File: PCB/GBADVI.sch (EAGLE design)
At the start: 77 parts, among them IC2 AMS1117-3.3V, IC3 AMS1117-1.2V, J1 47151-1081HDMI-001, Q1 IRF7319TR, U1 W25Q64JVSSIQ, U2 SN74LVC245APWR, U3 SN74LVC245APWR, U4 52271-1469, U5 FH12A-40S-0.5SH(55), U7 MT48LC16M16A2TG-6A_IT:GTR

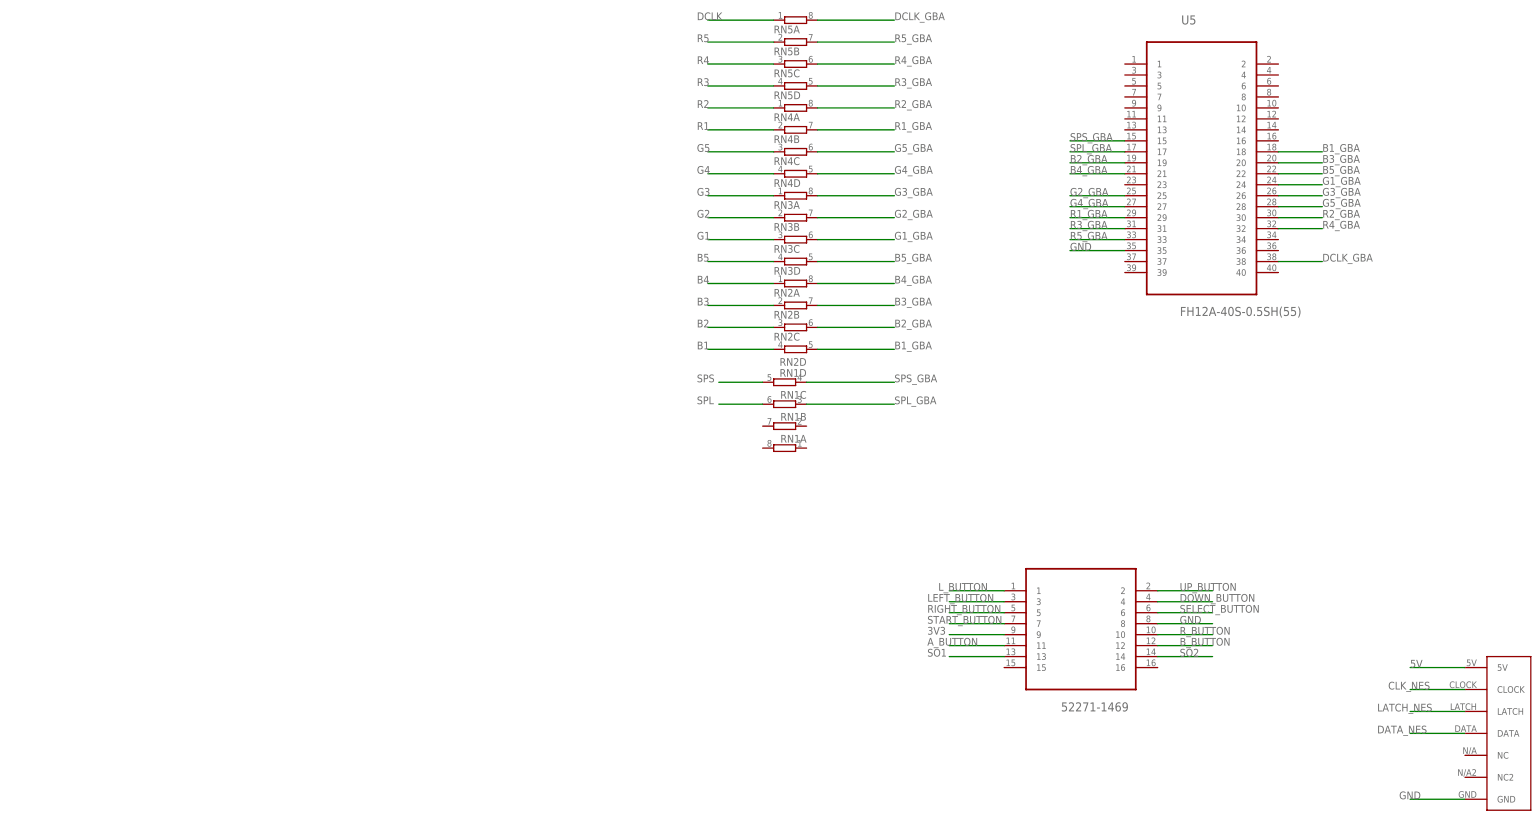
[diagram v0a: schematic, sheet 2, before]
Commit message: Updated board for i2c EEPROM and added WS2812B LEDs
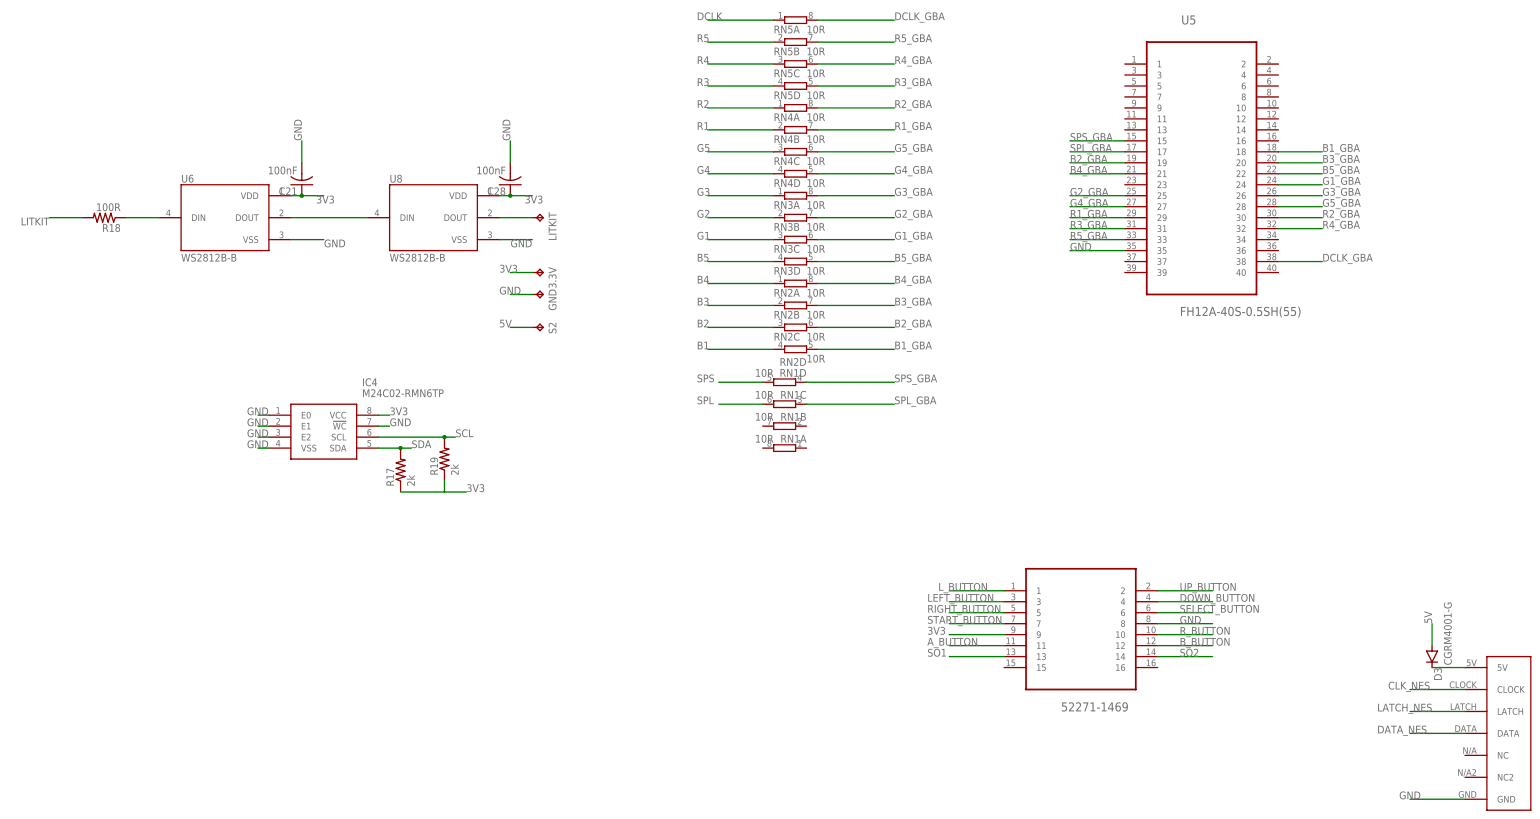
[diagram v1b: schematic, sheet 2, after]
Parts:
- added 3.3V, GND, LITKIT, S2: TPB1,27, testpad:TPB1,27
- added C21, C28: 100nF, adafruit:C-USC0603
- added D3: CGRM4001-G, diode:CGRM4001-G
- added IC4: M24C02-RMN6TP, M24C02-RMN6TP:M24C02-RMN6TP
- added R17, R19: 2k, rcl:R-US_R0603
- added R18: 100R, rcl:R-US_R0603
- added U6, U8: WS2812B-B, WS2812B-B:WS2812B-B
- RN1, RN2, RN3, RN4, RN5: value (none) -> 10R
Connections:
- new net LITKIT: R18.2, U$2.IO_L44P_GCLK21_3
- new net N$14: R18.1, U6.DIN
- new net N$16: U6.DOUT, U8.DIN
- new net N$22: LITKIT.TP, U8.DOUT
- new net N$8: D3.C, U$3.5V
- new net SCL: IC4.SCL, R19.2, U$2.IO_L43P_GCLK23_3
- new net SDA: IC4.SDA, R17.2, U$2.IO_L43N_GCLK22_IRDY2_3
- net 3V3: now also 3.3V.TP, C21.1, C28.1, IC4.VCC, R17.1, R19.1, U6.VDD, U8.VDD
- net 5V: now also D3.A, S2.TP; no longer U$3.5V
- net GND: now also C21.2, C28.2, GND.TP, IC4.!WC, IC4.E0, IC4.E1, IC4.E2, IC4.VSS, U6.VSS, U8.VSS
